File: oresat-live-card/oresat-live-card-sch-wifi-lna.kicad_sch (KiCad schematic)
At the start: 34 parts, among them J12 U.FL, J14 Conn_01x02, U18 TQP3M9037, U27 PAT1220-C-3DB, U28 PD2328J5050S2HF, U29 LTC5538

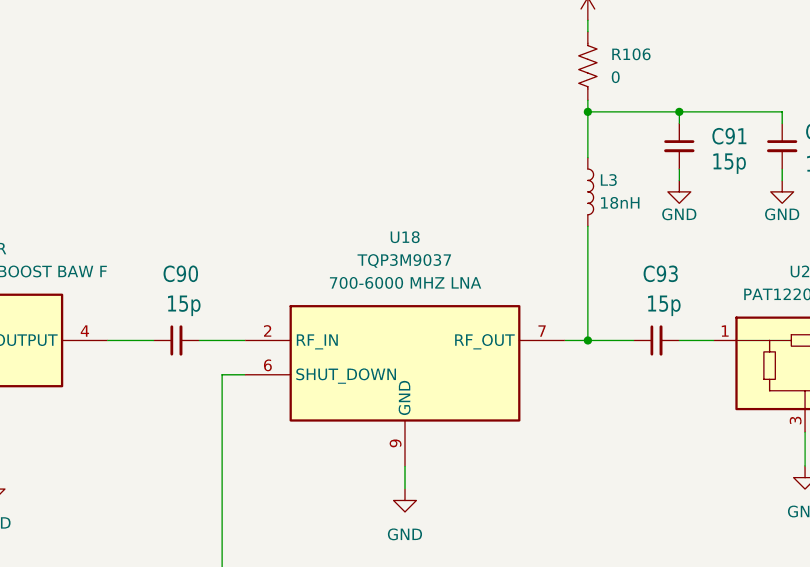
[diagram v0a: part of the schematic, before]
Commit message: added Olivers BOM and footprint changes, cleaned up pcb
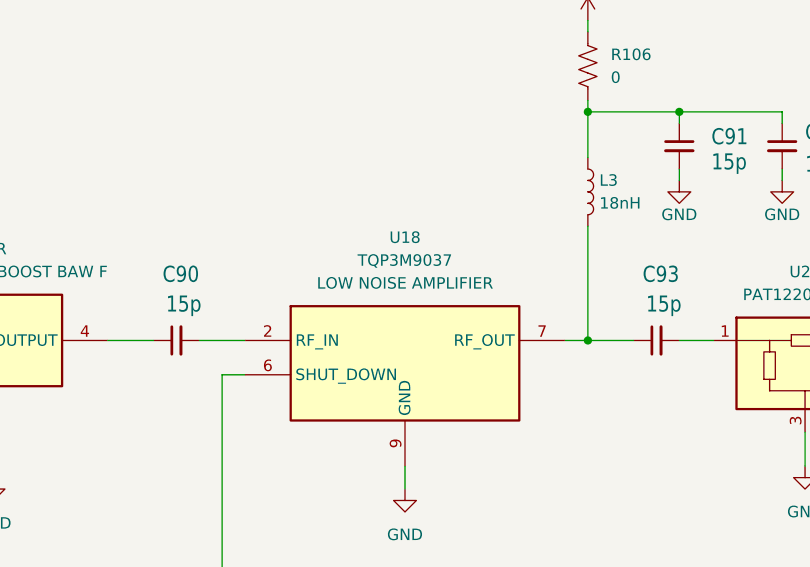
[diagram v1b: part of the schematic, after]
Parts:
- C106, C111, R105, R118, R119, R120, R121, R85, R88: footprint Resistor_SMD:R_0603_1608Metric -> oresat-passives:0603-C
- C107, C108, C109, C110, C114, L4: footprint Resistor_SMD:R_0402_1005Metric -> oresat-passives:0402-C
- C112, C113: footprint Resistor_SMD:R_0402_1005Metric -> oresat-passives:0402-C; DPN 445-5667-1-ND -> 445-6902-1-ND; MPN CGA3E2X7R1E104K080AA -> CGA2B3X7R1E104K050BB
- C90, C93: footprint oresat-passives:0402-C-NOSILK -> oresat-passives:0402-C
- C91: footprint Capacitor_SMD:C_0402_1005Metric -> oresat-passives:0402-C
- C92: footprint Capacitor_SMD:C_0402_1005Metric -> oresat-passives:0402-C; DPN 445-12539-1-ND -> 587-3709-1-ND; MFR TDK Corporation -> Taiyo Yuden; MPN CGA3E1X7R1C105K080AC -> EMK105BJ105KVHF
- L3: DIS (none) -> DigiKey; DPN 994-0603DC-18NXJRW -> 2457-0603DC-18NXJRW-ND
- R106: footprint Capacitor_SMD:C_0402_1005Metric -> oresat-passives:0402-C; DPN P0.0GCT-ND -> P0.0JCT-ND; MPN ERJ-3GEY0R00V -> ERJ-2GE0R00X
- R109: footprint Resistor_SMD:R_0603_1608Metric -> oresat-passives:0603-C; DPN P100HCT-ND -> P56.0HCT-ND; MPN ERJ-3EKF1000V -> ERJ-3EKF56R0V
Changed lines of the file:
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@@
 			)
 		)
-		(property "Footprint" "Resistor_SMD:R_0402_1005Metric"
+		(property "Footprint" "oresat-passives:0402-C"
 			(at 311.15 99.06 0)
 			(effects
@@
 			)
 		)
-		(property "Footprint" "Resistor_SMD:R_0402_1005Metric"
+		(property "Footprint" "oresat-passives:0402-C"
 			(at 337.82 154.94 0)
 			(effects
@@
 			)
 		)
-		(property "Footprint" "Resistor_SMD:R_0603_1608Metric"
+		(property "Footprint" "oresat-passives:0603-C"
 			(at 66.04 119.38 0)
 			(effects
@@
 			)
 		)
-		(property "Footprint" "Resistor_SMD:R_0402_1005Metric"
+		(property "Footprint" "oresat-passives:0402-C"
 			(at 326.39 149.86 0)
 			(effects
@@
 			)
 		)
-		(property "Description" "CAP CER 0.1UF 25V X7R 0603"
+		(property "Description" "CAP CER 0.1UF 25V X7R 0402"
 			(at 326.39 149.86 0)
 			(effects
@@
 			)
 		)
-		(property "DPN" "445-5667-1-ND "
+		(property "DPN" "445-6902-1-ND"
 			(at 326.39 149.86 90)
 			(effects
@@
 			)
 		)
-		(property "MPN" "CGA3E2X7R1E104K080AA "
+		(property "MPN" "CGA2B3X7R1E104K050BB"
 			(at 326.39 149.86 90)
 			(effects
@@
 			)
 		)
-		(property "Footprint" "Resistor_SMD:R_0603_1608Metric"
+		(property "Footprint" "oresat-passives:0603-C"
 			(at 369.57 129.54 0)
 			(effects
@@
 			)
 		)
-		(property "Footprint" "Capacitor_SMD:C_0402_1005Metric"
+		(property "Footprint" "oresat-passives:0402-C"
 			(at 138.43 54.61 0)
 			(effects
@@
 			)
 		)
-		(property "Footprint" "Resistor_SMD:R_0402_1005Metric"
+		(property "Footprint" "oresat-passives:0402-C"
 			(at 245.11 146.05 0)
 			(effects
@@
 			)
 		)
-		(property "Footprint" "Resistor_SMD:R_0603_1608Metric"
+		(property "Footprint" "oresat-passives:0603-C"
 			(at 258.826 147.574 90)
 			(effects
@@
 			)
 		)
-		(property "Description" "RES SMD 100 OHM 1% 1/10W 0603"
+		(property "Description" "RES SMD 56 OHM 1% 1/10W 0603"
 			(at 257.81 147.32 0)
 			(effects
@@
 			)
 		)
-		(property "DPN" "P100HCT-ND "
+		(property "DPN" "P56.0HCT-ND"
 			(at 257.81 147.32 0)
 			(effects
@@
 			)
 		)
-		(property "MPN" "ERJ-3EKF1000V"
+		(property "MPN" "ERJ-3EKF56R0V"
 			(at 257.81 147.32 0)
 			(effects
@@
 			)
 		)
-		(property "Footprint" "Resistor_SMD:R_0603_1608Metric"
+		(property "Footprint" "oresat-passives:0603-C"
 			(at 80.264 112.014 90)
 			(effects
@@
 			)
 		)
-		(property "Footprint" "Resistor_SMD:R_0402_1005Metric"
+		(property "Footprint" "oresat-passives:0402-C"
 			(at 266.7 137.16 0)
 			(effects
@@
 			)
 		)
-		(property "Datasheet" "~"
+		(property "Datasheet" ""
 			(at 266.7 137.16 0)
 			(effects
@@
 			)
 		)
-		(property "DPN" "994-0603DC-18NXJRW"
+		(property "DPN" "2457-0603DC-18NXJRW-ND"
 			(at 128.27 59.69 0)
 			(effects
@@
 			)
 		)
-		(property "DIS" ""
+		(property "DIS" "DigiKey"
 			(at 128.27 59.69 0)
 			(effects
@@
 			)
 		)
-		(property "Footprint" "Resistor_SMD:R_0402_1005Metric"
+		(property "Footprint" "oresat-passives:0402-C"
 			(at 278.13 148.59 0)
 			(effects
@@
 			)
 		)
-		(property "Datasheet" "~"
+		(property "Datasheet" ""
 			(at 278.13 148.59 0)
 			(effects
@@
 			)
 		)
-		(property "Footprint" "Resistor_SMD:R_0603_1608Metric"
+		(property "Footprint" "oresat-passives:0603-C"
 			(at 345.694 119.634 90)
 			(effects
@@
 			)
 		)
-		(property "Footprint" "Resistor_SMD:R_0603_1608Metric"
+		(property "Footprint" "oresat-passives:0603-C"
 			(at 88.646 122.174 90)
 			(effects
@@
 			)
 		)
-		(property "Footprint" "oresat-passives:0402-C-NOSILK"
+		(property "Footprint" "oresat-passives:0402-C"
 			(at 82.55 76.2 0)
 			(effects
@@
 			)
 		)
-		(property "Description" "700-6000 MHZ LNA"
+		(property "Description" "LOW NOISE AMPLIFIER"
 			(at 107.95 69.85 0)
 			(effects
@@
 			)
 		)
-		(property "Footprint" "Resistor_SMD:R_0402_1005Metric"
+		(property "Footprint" "oresat-passives:0402-C"
 			(at 251.46 137.16 0)
 			(effects
@@
 			)
 		)
-		(property "Footprint" "Capacitor_SMD:C_0402_1005Metric"
+		(property "Footprint" "oresat-passives:0402-C"
 			(at 149.86 54.61 0)
 			(effects
@@
 			)
 		)
-		(property "Description" "CAP CER 1UF 16V X7R 0603"
+		(property "Description" "CAP CER 1UF 16V X5R 0402"
 			(at 149.86 54.61 0)
 			(effects
@@
 			)
 		)
-		(property "MPN" "CGA3E1X7R1C105K080AC "
+		(property "MPN" "EMK105BJ105KVHF"
 			(at 149.86 54.61 0)
 			(effects
@@
 			)
 		)
-		(property "DPN" "445-12539-1-ND "
+		(property "DPN" "587-3709-1-ND"
 			(at 149.86 54.61 0)
 			(effects
@@
 			)
 		)
-		(property "MFR" "TDK Corporation "
+		(property "MFR" "Taiyo Yuden"
 			(at 149.86 54.61 0)
 			(effects
@@
 			)
 		)
-		(property "Footprint" "oresat-passives:0402-C-NOSILK"
+		(property "Footprint" "oresat-passives:0402-C"
 			(at 135.89 76.2 0)
 			(effects
@@
 			)
 		)
-		(property "Footprint" "Resistor_SMD:R_0402_1005Metric"
+		(property "Footprint" "oresat-passives:0402-C"
 			(at 326.39 137.16 0)
 			(effects
@@
 			)
 		)
-		(property "Description" "CAP CER 0.1UF 25V X7R 0603"
+		(property "Description" "CAP CER 0.1UF 25V X7R 0402"
 			(at 326.39 137.16 0)
 			(effects
@@
 			)
 		)
-		(property "DPN" "445-5667-1-ND "
+		(property "DPN" "445-6902-1-ND"
 			(at 326.39 137.16 90)
 			(effects
@@
 			)
 		)
-		(property "MPN" "CGA3E2X7R1E104K080AA "
+		(property "MPN" "CGA2B3X7R1E104K050BB"
 			(at 326.39 137.16 90)
 			(effects
@@
 			)
 		)
-		(property "Footprint" "Resistor_SMD:R_0603_1608Metric"
+		(property "Footprint" "oresat-passives:0603-C"
 			(at 311.15 109.22 0)
 			(effects
@@
 			)
 		)
-		(property "Footprint" "Resistor_SMD:R_0603_1608Metric"
+		(property "Footprint" "oresat-passives:0603-C"
 			(at 279.146 124.714 90)
 			(effects
@@
 			)
 		)
-		(property "Footprint" "Resistor_SMD:R_0603_1608Metric"
+		(property "Footprint" "oresat-passives:0603-C"
 			(at 246.126 78.994 90)
 			(effects
@@
 			)
 		)
-		(property "Footprint" "Resistor_SMD:R_0603_1608Metric"
+		(property "Footprint" "oresat-passives:0603-C"
 			(at 355.854 129.286 90)
 			(effects
@@
 			)
 		)
-		(property "Footprint" "Capacitor_SMD:C_0402_1005Metric"
+		(property "Footprint" "oresat-passives:0402-C"
 			(at 127.254 45.466 90)
 			(effects
@@
 			)
 		)
-		(property "Description" "RES SMD 0 OHM JUMPER 1/10W 0603"
+		(property "Description" "RES SMD 0 OHM JUMPER 1/10W 0402"
 			(at 128.27 45.72 0)
 			(effects
@@
 			)
 		)
-		(property "DPN" "P0.0GCT-ND "
+		(property "DPN" "P0.0JCT-ND"
 			(at 128.27 45.72 0)
 			(effects
@@
 			)
 		)
-		(property "MPN" "ERJ-3GEY0R00V "
+		(property "MPN" "ERJ-2GE0R00X"
 			(at 128.27 45.72 0)
 			(effects

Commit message: added 100p cap to U34 CTRL line, some BOM changes
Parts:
- R85: DPN ERJ-3EKF4701V -> P4.70KHCT-ND
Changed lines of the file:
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@@
 			)
 		)
-		(property "DPN" "ERJ-3EKF4701V"
+		(property "DPN" "P4.70KHCT-ND"
 			(at 66.04 119.38 0)
 			(effects
